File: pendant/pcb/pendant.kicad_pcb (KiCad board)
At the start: 2 copper layers, 96.2 x 129.6 mm, 59 parts, among them CN1 S2B-PH-SM4-TB(LF)(SN), CN2 S4B-PH-SM4-TB(LF)(SN), Q1 DMG3415U-7, SW1 TS-1088-AR02016, SW2 TS-1088-AR02016, U1 ESP32-S3-WROOM-1, U2 TCA8418RTWR, U3 TPS61169DCKR, U5 APX803S-26SA-7, U6 MCP73831T-2ACI/OT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

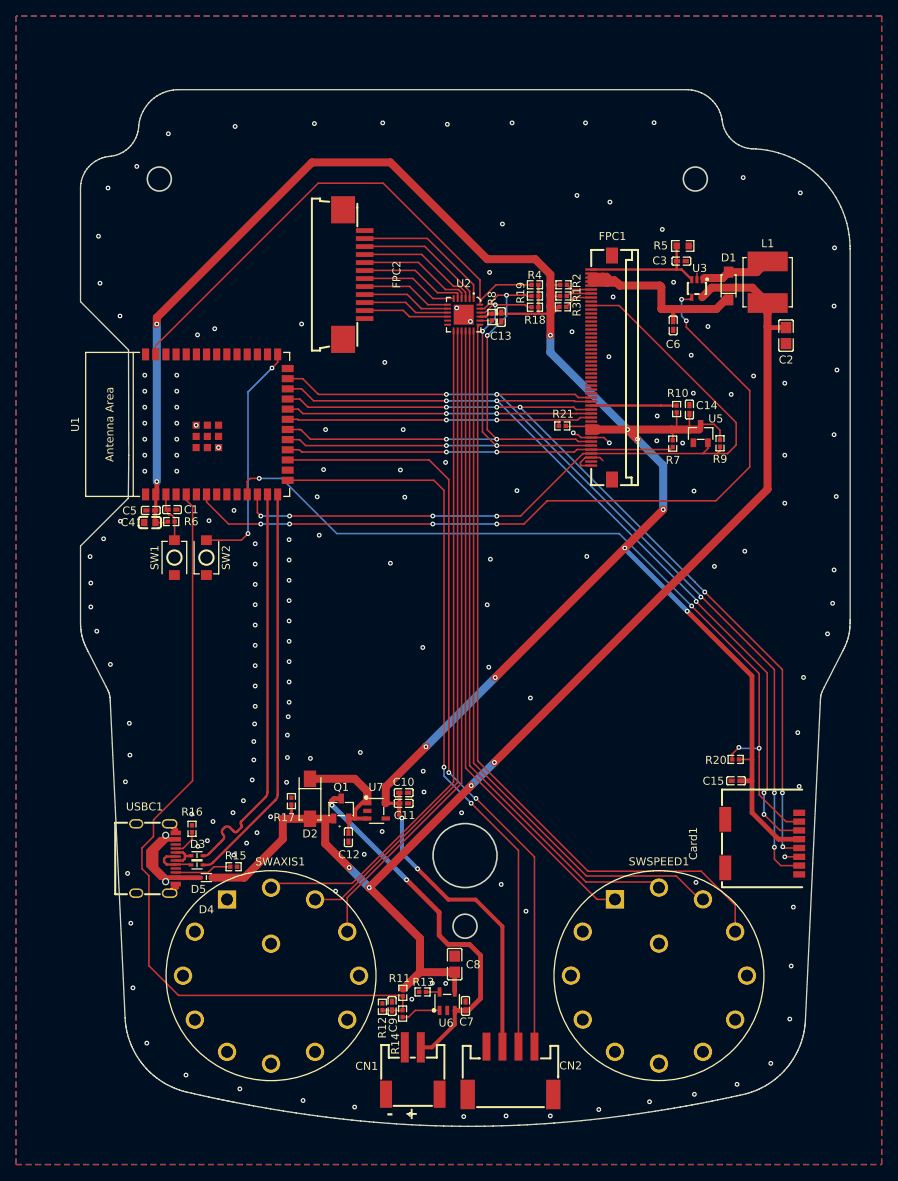
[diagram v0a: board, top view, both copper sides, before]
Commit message: fix errors on pendant pcb
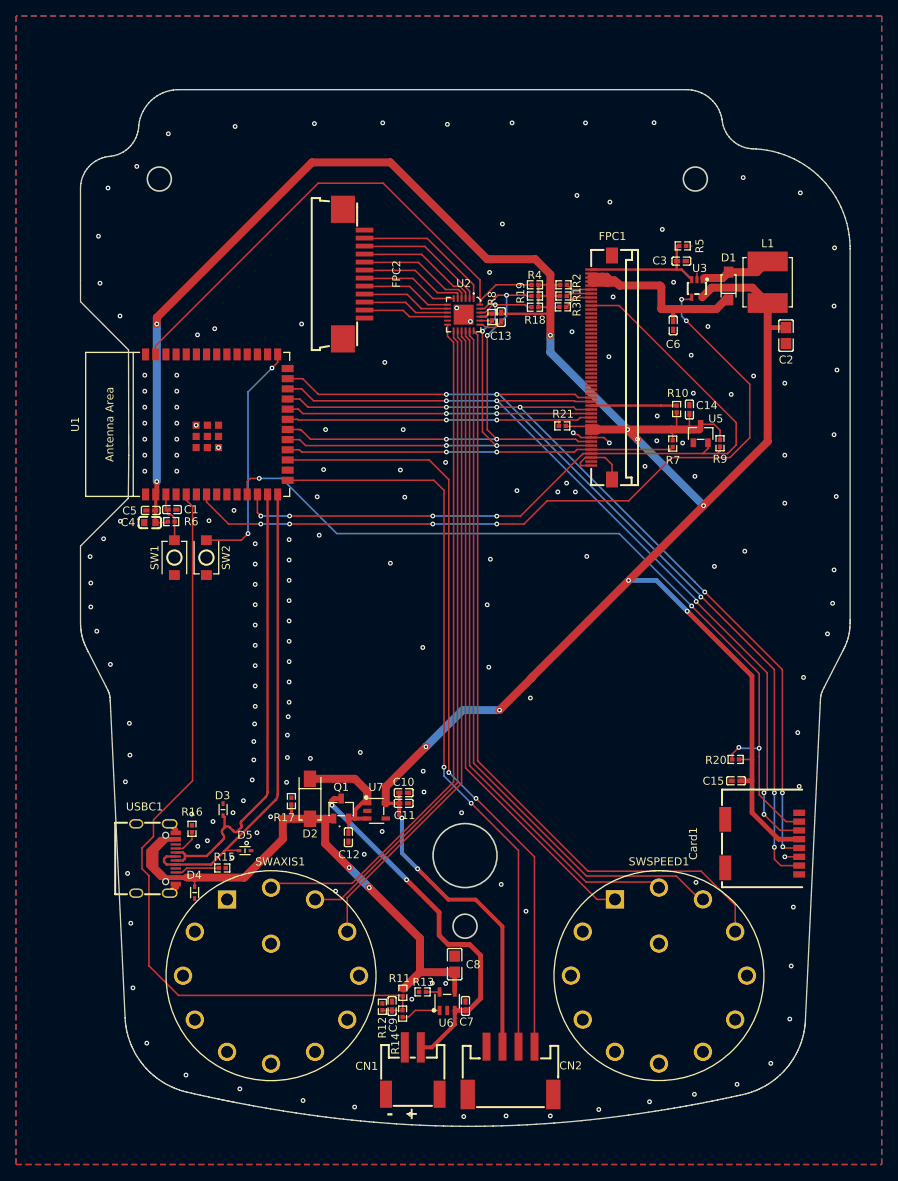
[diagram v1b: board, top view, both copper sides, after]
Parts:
- R5: footprint pendant:R0603 -> pendant:R0402
- moved D3 6.62 mm to (80.2, 124.5), turned to -90 degrees
- moved D5 6.26 mm to (82.9, 129.6), turned to 0 degrees
- moved D4 2.38 mm to (76.6, 134.9), turned to 90 degrees
- moved R15 1.42 mm to (80.1, 131.8)
- moved FPC2 0.06 mm to (96.5, 57.6)
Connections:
- C2 pad 2: VBUS -> 3V3
- D3 pad 1: D- -> GND
- D3 pad 2: /DN1 -> D-
- D4 pad 1: VBUS -> GND
- D4 pad 2: /VBUSD -> VBUS
- D5 pad 2: /DP1 -> GND
- L1 pad 2: VBUS -> 3V3
- U2 pad 12: unconnected-(U2-COL3-Pad12) -> AXIS_X
- U2 pad 13: AXIS_X -> AXIS_Y
- U2 pad 14: AXIS_Y -> AXIS_Z
- U2 pad 15: AXIS_Z -> SPEED_1
- U2 pad 16: SPEED_1 -> SPEED_2
- U2 pad 17: SPEED_2 -> SPEED_3
- U2 pad 18: SPEED_3 -> SPEED_4
- U2 pad 19: SPEED_4 -> GND
- U3 pad 5: VBUS -> 3V3
- USBC1 pad A4: /VBUSD -> VBUS
- USBC1 pad A6: /DP1 -> D+
- USBC1 pad A7: /DN1 -> D-
- USBC1 pad A9: /VBUSD -> VBUS
- USBC1 pad B4: /VBUSD -> VBUS
- USBC1 pad B6: /DP1 -> D+
- USBC1 pad B7: /DN1 -> D-
- USBC1 pad B9: /VBUSD -> VBUS
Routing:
- net VBUS: track 160.4 -> 59.4 mm, vias 4 -> 2
- net 3V3: track 312.5 -> 363.2 mm
- net D+: track 50.7 -> 59.6 mm
- net D-: track 50.6 -> 57.5 mm
- net GND: track 15.3 -> 21.7 mm, vias 172 -> 176
- net /DP1: track 5.41 -> 0.00 mm
- net /DN1: track 3.79 -> 0.00 mm
- net /VBUSD: track 2.92 -> 0.00 mm
- net LCD_LITE: track 98.8 -> 96.7 mm
- net Net-(USBC1-CC2): track 7.10 -> 5.62 mm
- net AXIS_X: track 83.9 -> 85.0 mm
- net SPEED_4: track 97.6 -> 96.9 mm

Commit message: update pendant pcb
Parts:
- added C16: 0.1uF, pendant:C0402, F.Cu at (96.3, 115.4)
- added R22: 10k, pendant:R0402, F.Cu at (94.0, 114.9)
- added U4: MAX17048G+T10, pendant:DFN-8_L2.0-W2.0-P0.50-BL-EP, F.Cu at (94.0, 117.2)
- C5: value 4.7uF 10V -> 4.7uF
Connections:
- CN1 pad 1: GND -> VBAT
- CN1 pad 2: VBAT -> GND
- SWAXIS1 pad 1: unconnected-(SWAXIS1-Pad1) -> AXIS_OFF
- U1 pad 10: unconnected-(U1-GPIO17/U1TXD/ADC2_CH6-Pad10) -> ALRT
- U2 pad 11: unconnected-(U2-COL2-Pad11) -> AXIS_OFF
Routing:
- net AXIS_OFF: track 0.00 -> 93.4 mm
- net SDA: track 64.3 -> 104.8 mm, vias 4 -> 6
- net ALRT: track 0.00 -> 40.4 mm, vias 0 -> 2
- net SCL: track 65.3 -> 105.4 mm, vias 4 -> 6
- net 3V3: track 363.2 -> 381.1 mm
- net VBAT: track 47.6 -> 60.6 mm, vias 2 -> 3
- net GND: track 21.7 -> 33.0 mm, vias 176 -> 181
- net 24V: track 31.5 -> 29.4 mm
- net BOOT: track 29.5 -> 27.6 mm
- net ROTARY_B: track 96.6 -> 95.4 mm
- net SD_CS: track 101.9 -> 100.9 mm
- net ROTARY_A: track 93.5 -> 92.9 mm
